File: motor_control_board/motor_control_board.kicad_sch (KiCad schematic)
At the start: 27 parts

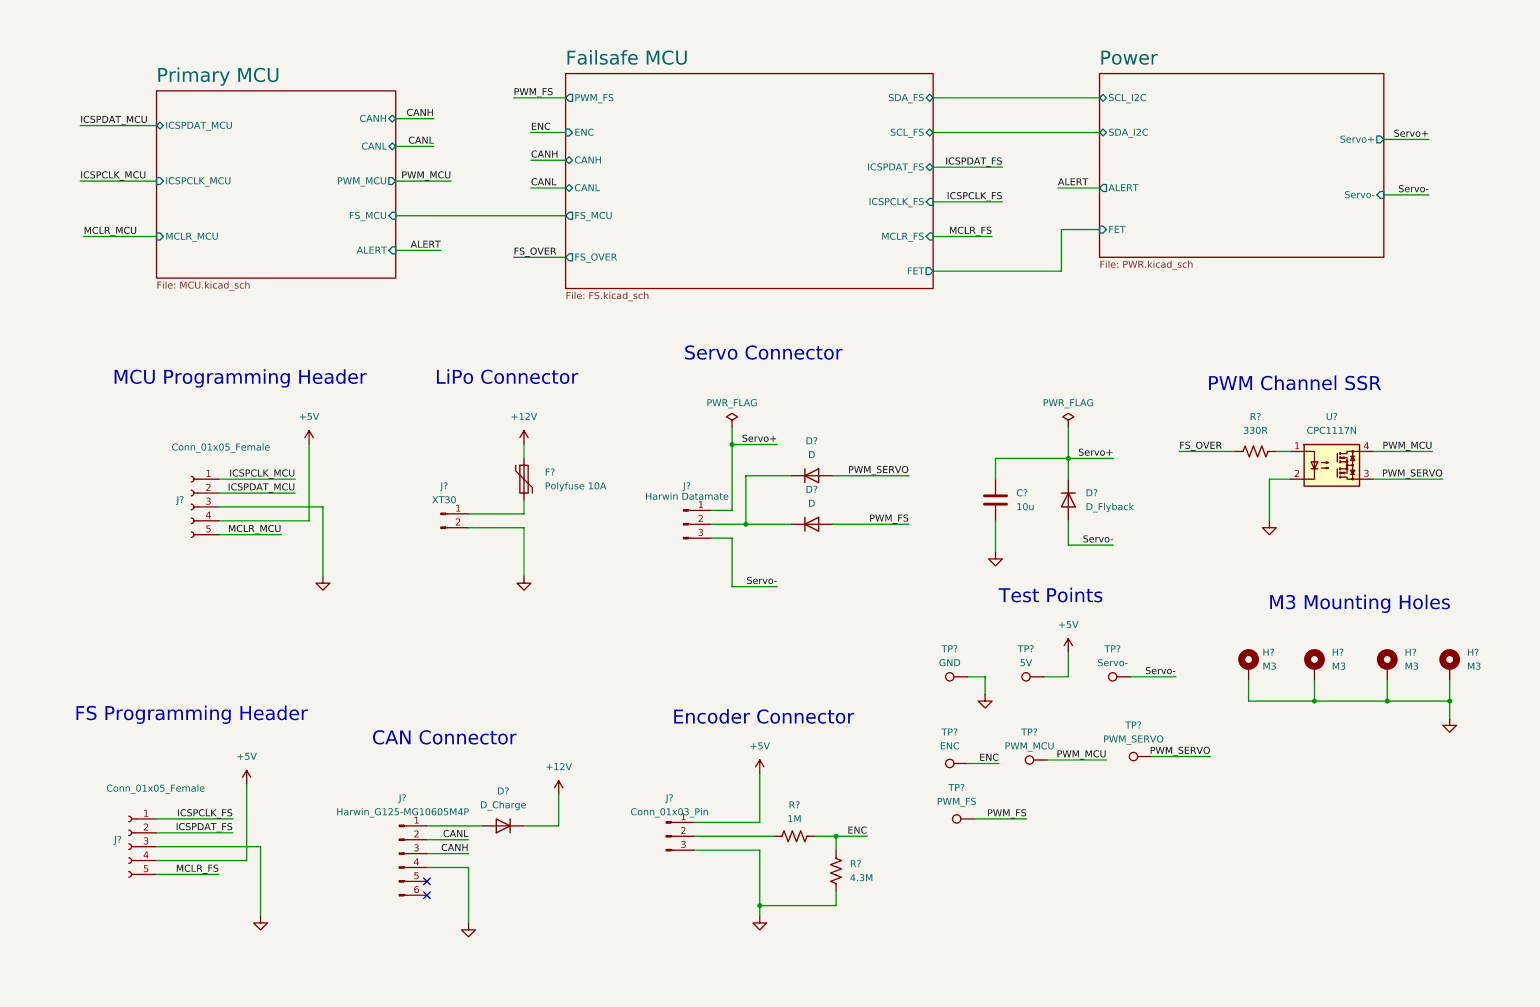
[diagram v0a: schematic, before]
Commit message: Minor schematic edits
Annotated schematic, selected mosfet and diodes, addressed comments
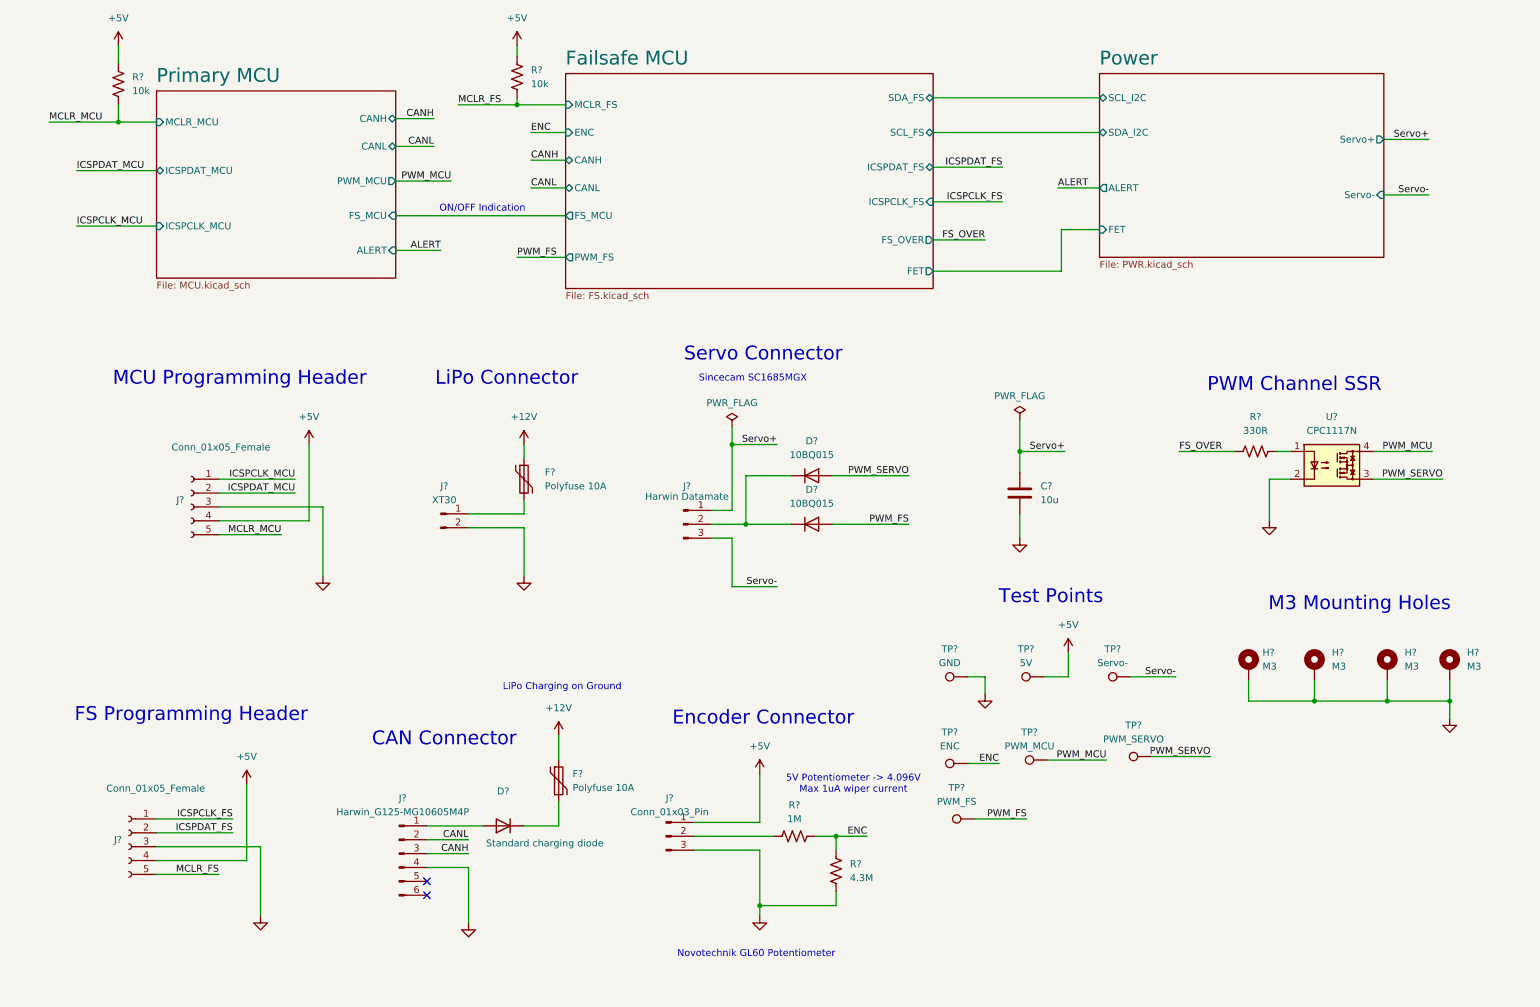
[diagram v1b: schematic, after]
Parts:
- removed D?: D_Flyback, symbol canhw:D
- added F?: Polyfuse 10A, symbol canhw:Polyfuse
- added R? (x2): 10k, symbol Device:R_US
- D? (x2): value D -> 10BQ015
- D?: value D_Charge -> Standard charging diode
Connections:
- net +12V: now also F?.1; no longer D?.1 (K)
- net +5V: now also R?.1, R?.1
- net MCLR_FS: now also R?.2
- net MCLR_MCU: now also R?.2
- new net: D?.1 (K), F?.2
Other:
- note added: "5V Potentiometer -> 4.096V Max 1uA wiper current"
- note added: "LiPo Charging on Ground"
- note added: "Novotechnik GL60 Potentiometer"
- note added: "ON/OFF Indication"
- note added: "Sincecam SC1685MGX"
- moved on the sheet: C?

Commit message: Added second encoder connection, minor edits
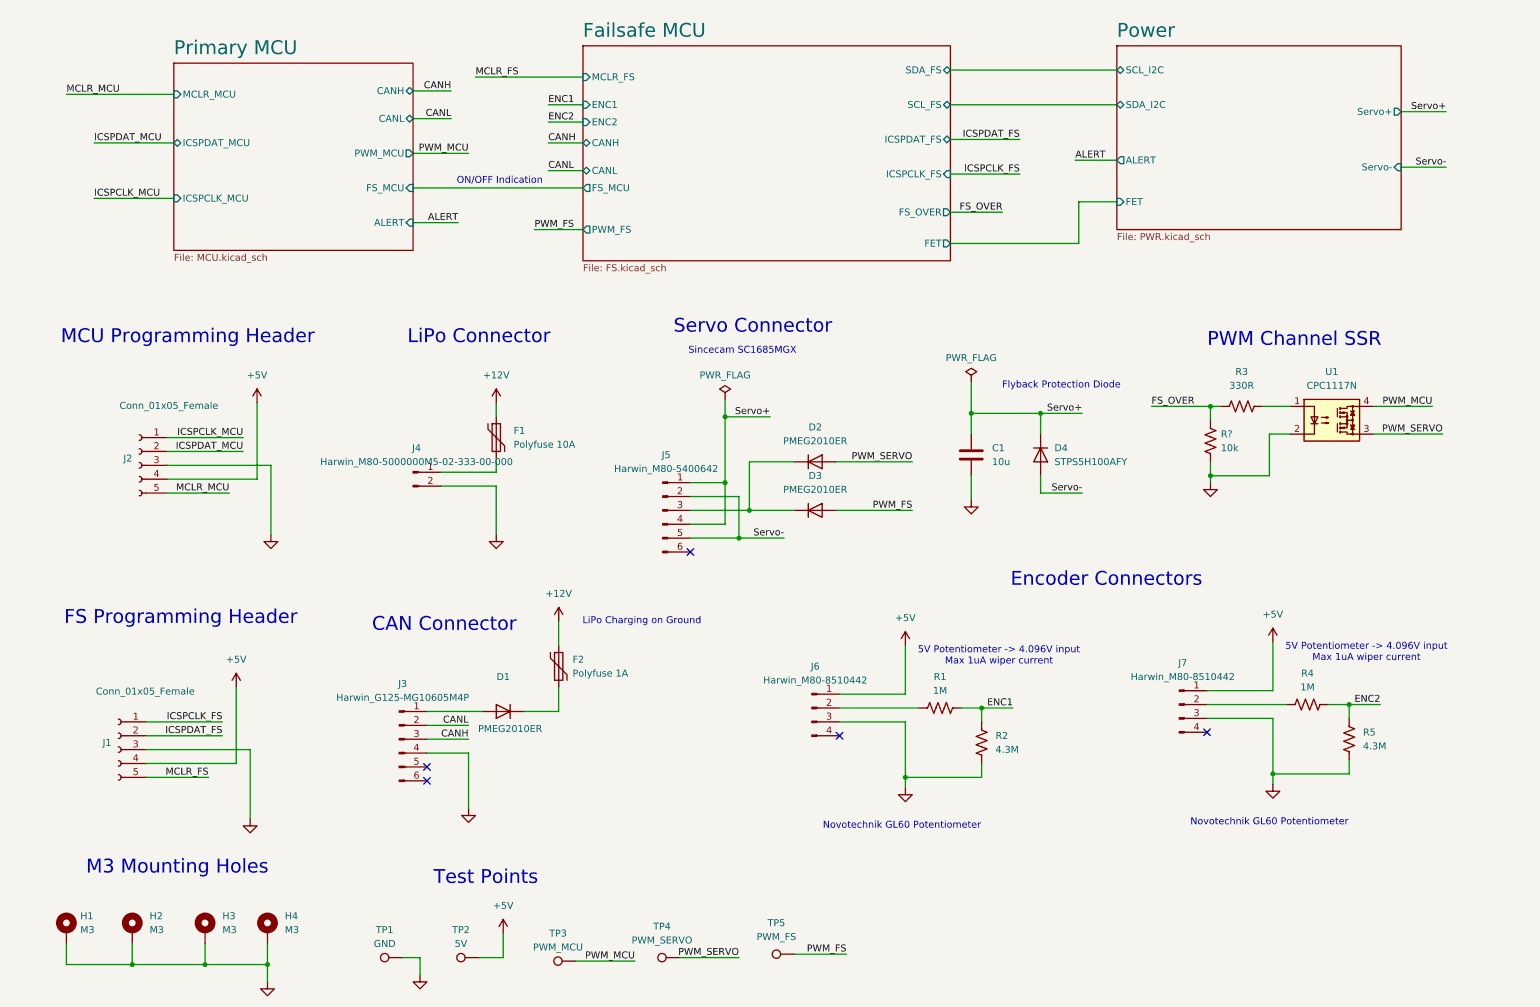
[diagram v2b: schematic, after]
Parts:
- removed J?: Conn_01x03_Pin, symbol canhw:Conn_01x03_Pin
- removed J?: Harwin Datamate, symbol canhw:Conn_01x03_Pin
- removed R? (x2): 10k, symbol Device:R_US
- removed TP?: Servo-, symbol canhw:TestPoint
- removed TP?: ENC, symbol canhw:TestPoint
- added D4: STPS5H100AFY, symbol canhw:D
- added J5: Harwin_M80-5400642, symbol canhw:Conn_01x06_Pin
- added J6, J7: Harwin_M80-8510442, symbol Connector:Conn_01x04_Pin
- added R4: 1M, symbol canhw:R_US
- added R5: 4.3M, symbol canhw:R_US
- added R?: 10k, symbol Device:R_US
- D1: renamed from D?; value Standard charging diode -> PMEG2010ER
- D2, D3: renamed from D?; value 10BQ015 -> PMEG2010ER
- F2: renamed from F?; value Polyfuse 10A -> Polyfuse 1A
- J4: renamed from J?; value XT30 -> Harwin_M80-5000000M5-02-333-00-000
- gave numbers to parts that had none: 18
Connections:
- net +5V: now also J6.1 (Pin_1), J7.1 (Pin_1)
- net FS_OVER: now also R?.1
- net GND: now also J6.3 (Pin_3), J7.3 (Pin_3), R5.2, R?.2
- net Servo+: now also D4.1 (K), J5.1 (Pin_1), J5.4 (Pin_4)
- net Servo-: now also D4.2 (A), J5.2 (Pin_2), J5.5 (Pin_5)
- net at R1.1: now also J6.2 (Pin_2)
- net at D2.1 (K), D3.1 (K): now also J5.3 (Pin_3)
- net ENC renamed ENC1
- new net: J7.2 (Pin_2), R4.1
- new net ENC2: R4.2, R5.1
- no-connect marks 2 -> 5
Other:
- sheet Failsafe MCU ports: added ENC1, ENC2; removed ENC
- note added: "5V Potentiometer -> 4.096V input Max 1uA wiper current"
- note added: "Encoder Connectors"
- note added: "Flyback Protection Diode"
- note removed: "5V Potentiometer -> 4.096V Max 1uA wiper current"
- note removed: "Encoder Connector"
- moved on the sheet: C1, D1, D2, D3, F1, F2, H1, H2, H3, H4, J1, J2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

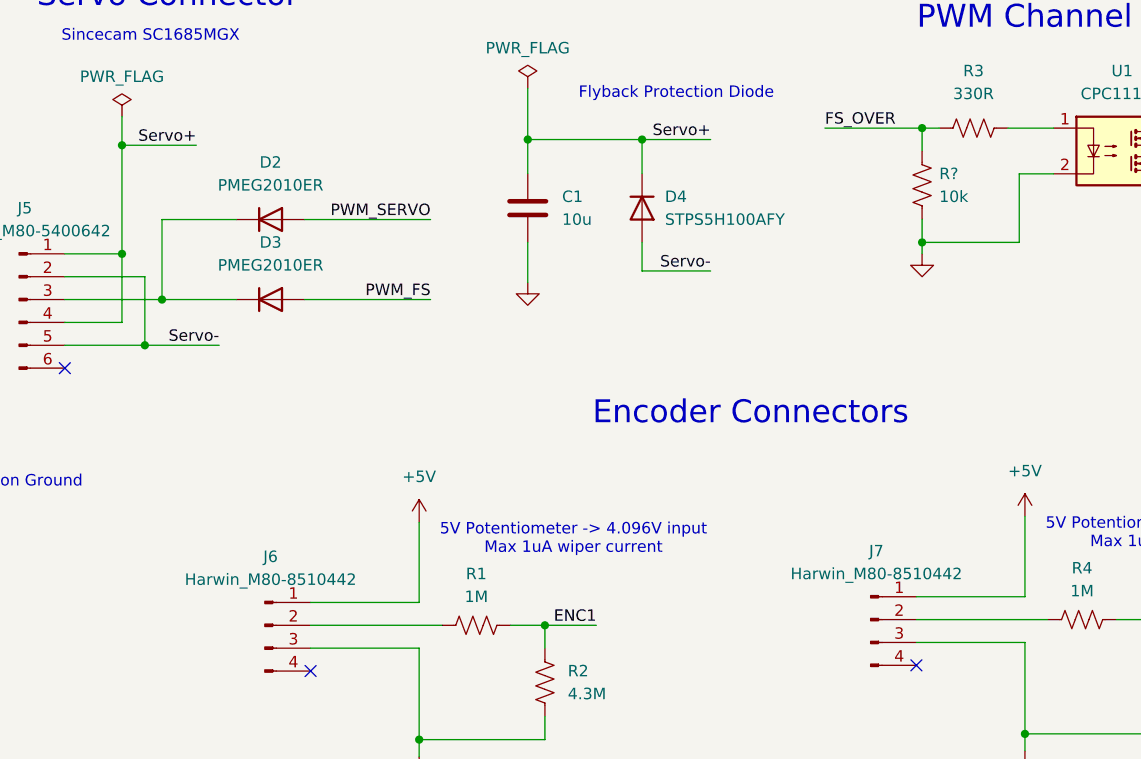
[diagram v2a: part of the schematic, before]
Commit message: assigned footprints
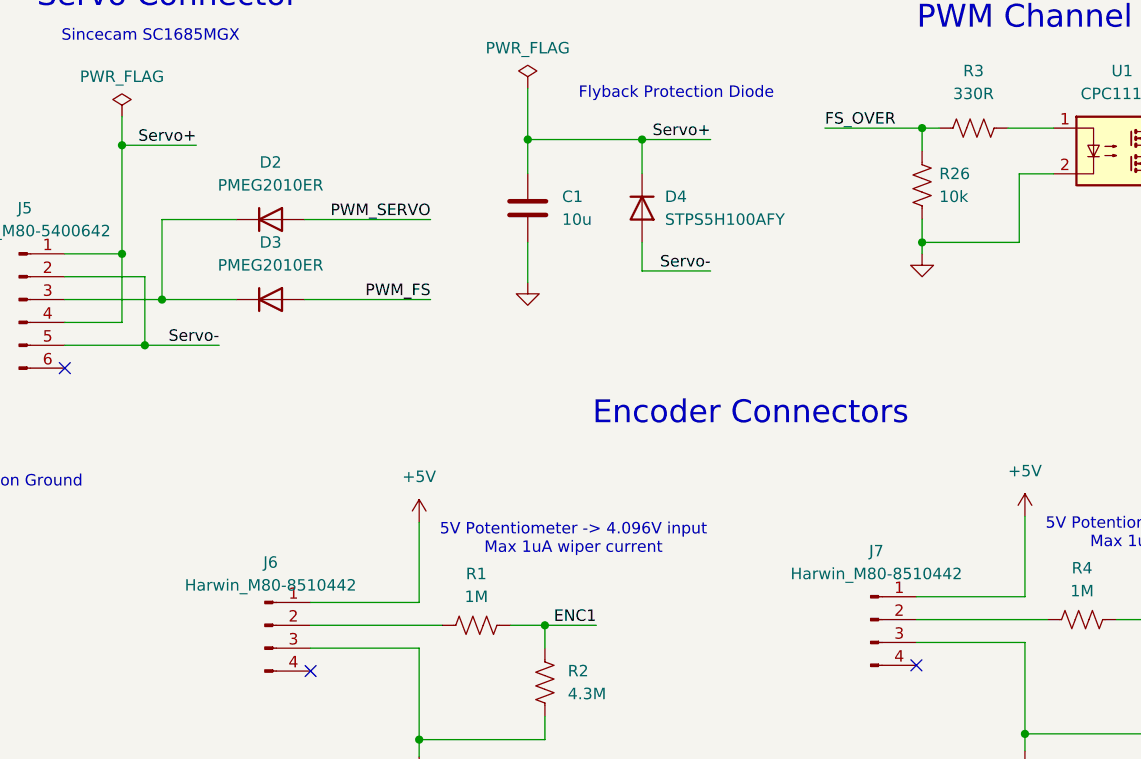
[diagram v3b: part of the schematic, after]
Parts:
- C1: footprint (none) -> Capacitor_SMD:C_0805_2012Metric_Pad1.18x1.45mm_HandSolder
- D1, D2, D3: footprint (none) -> Diode_SMD:Nexperia_CFP3_SOD-123W
- D4: footprint (none) -> Diode_SMD:D_SOD-128
- F1, F2: footprint (none) -> Fuse:Fuse_1206_3216Metric_Pad1.42x1.75mm_HandSolder
- H1, H2, H3, H4: footprint (none) -> MountingHole:MountingHole_3.2mm_M3_DIN965_Pad
- J1, J2: footprint (none) -> canhw_footprints:PinSocket_5x2.54_SMD_90deg_952-3198-1-ND
- J3: footprint (none) -> canhw_footprints:connector_Harwin_G125–MG10605M4P
- J4: footprint (none) -> motor-control:HARWIN_M80-5000000M5-02-333-00-000
- J5: footprint (none) -> motor-control:HARWIN_M80-5400642
- J6, J7: footprint (none) -> motor-control:HARWIN_M80-8510442
- R1, R2, R3, R4, R5: footprint (none) -> Resistor_SMD:R_0805_2012Metric_Pad1.20x1.40mm_HandSolder
- R26: renamed from R?; footprint (none) -> Resistor_SMD:R_0805_2012Metric_Pad1.20x1.40mm_HandSolder
- TP1, TP2, TP3, TP4, TP5: footprint (none) -> TestPoint:TestPoint_Keystone_5000-5004_Miniature
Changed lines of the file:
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@@
 			)
 		)
-		(property "Footprint" ""
+		(property "Footprint" "Fuse:Fuse_1206_3216Metric_Pad1.42x1.75mm_HandSolder"
 			(at 99.695 97.155 0)
 			(effects
@@
 			)
 		)
-		(property "Footprint" ""
+		(property "Footprint" "TestPoint:TestPoint_Keystone_5000-5004_Miniature"
 			(at 153.035 181.61 0)
 			(effects
@@
 			)
 		)
-		(property "Footprint" ""
+		(property "Footprint" "MountingHole:MountingHole_3.2mm_M3_DIN965_Pad"
 			(at 56.515 182.245 0)
 			(effects
@@
 			)
 		)
-		(property "Footprint" ""
+		(property "Footprint" "motor-control:HARWIN_M80-8510442"
 			(at 223.52 140.97 0)
 			(effects
@@
 			)
 		)
-		(property "Footprint" ""
+		(property "Footprint" "motor-control:HARWIN_M80-5000000M5-02-333-00-000"
 			(at 83.185 98.425 0)
 			(effects
@@
 			)
 		)
-		(property "Footprint" ""
+		(property "Footprint" "Fuse:Fuse_1206_3216Metric_Pad1.42x1.75mm_HandSolder"
 			(at 111.125 139.065 0)
 			(effects
@@
 			)
 		)
-		(property "Footprint" ""
+		(property "Footprint" "TestPoint:TestPoint_Keystone_5000-5004_Miniature"
 			(at 95.25 182.245 0)
 			(effects
@@
 		(dnp no)
 		(fields_autoplaced yes)
-		(property "Reference" "R?"
+		(property "Reference" "R26"
 			(at 231.14 91.4399 0)
 			(effects
@@
 			)
 		)
-		(property "Footprint" ""
+		(property "Footprint" "Resistor_SMD:R_0805_2012Metric_Pad1.20x1.40mm_HandSolder"
 			(at 230.251 92.964 90)
 			(effects
@@
 			(project ""
 				(path "/ced26b11-410b-4897-bfe1-68b095b3fef4"
-					(reference "R?")
+					(reference "R26")
 					(unit 1)
 				)
@@
 			)
 		)
-		(property "Footprint" ""
+		(property "Footprint" "Diode_SMD:Nexperia_CFP3_SOD-123W"
 			(at 156.845 105.41 0)
 			(effects
@@
 		(fields_autoplaced yes)
 		(property "Reference" "J6"
-			(at 156.845 133.985 0)
+			(at 156.845 134.62 0)
 			(effects
 				(font
@@
 		)
 		(property "Value" "Harwin_M80-8510442"
-			(at 156.845 136.525 0)
+			(at 156.845 137.16 0)
 			(effects
 				(font
@@
 			)
 		)
-		(property "Footprint" ""
+		(property "Footprint" "motor-control:HARWIN_M80-8510442"
 			(at 156.21 141.605 0)
 			(effects
@@
 			)
 		)
-		(property "Footprint" ""
+		(property "Footprint" "canhw_footprints:PinSocket_5x2.54_SMD_90deg_952-3198-1-ND"
 			(at 33.02 97.155 0)
 			(effects
@@
 			)
 		)
-		(property "Footprint" ""
+		(property "Footprint" "MountingHole:MountingHole_3.2mm_M3_DIN965_Pad"
 			(at 31.75 182.245 0)
 			(effects
@@
 			)
 		)
-		(property "Footprint" ""
+		(property "Footprint" "canhw_footprints:connector_Harwin_G125–MG10605M4P"
 			(at 80.645 147.32 0)
 			(effects
@@
 			)
 		)
-		(property "Footprint" ""
+		(property "Footprint" "MountingHole:MountingHole_3.2mm_M3_DIN965_Pad"
 			(at 45.085 182.245 0)
 			(effects
@@
 			)
 		)
-		(property "Footprint" ""
+		(property "Footprint" "MountingHole:MountingHole_3.2mm_M3_DIN965_Pad"
 			(at 19.685 182.245 0)
 			(effects
@@
 			)
 		)
-		(property "Footprint" ""
+		(property "Footprint" "Resistor_SMD:R_0805_2012Metric_Pad1.20x1.40mm_HandSolder"
 			(at 255.651 147.574 90)
 			(effects
@@
 			)
 		)
-		(property "Footprint" ""
+		(property "Footprint" "Diode_SMD:Nexperia_CFP3_SOD-123W"
 			(at 99.695 142.24 0)
 			(effects
@@
 			)
 		)
-		(property "Footprint" ""
+		(property "Footprint" "motor-control:HARWIN_M80-5400642"
 			(at 128.905 105.41 0)
 			(effects
@@
 			)
 		)
-		(property "Footprint" ""
+		(property "Footprint" "TestPoint:TestPoint_Keystone_5000-5004_Miniature"
 			(at 81.28 182.245 0)
 			(effects
@@
 			)
 		)
-		(property "Footprint" ""
+		(property "Footprint" "TestPoint:TestPoint_Keystone_5000-5004_Miniature"
 			(at 113.03 182.88 0)
 			(effects
@@
 			)
 		)
-		(property "Footprint" ""
+		(property "Footprint" "Diode_SMD:Nexperia_CFP3_SOD-123W"
 			(at 156.845 96.52 0)
 			(effects
@@
 			)
 		)
-		(property "Footprint" ""
+		(property "Footprint" "TestPoint:TestPoint_Keystone_5000-5004_Miniature"
 			(at 132.08 182.245 0)
 			(effects
@@
 			)
 		)
-		(property "Footprint" ""
+		(property "Footprint" "Resistor_SMD:R_0805_2012Metric_Pad1.20x1.40mm_HandSolder"
 			(at 235.204 85.344 90)
 			(effects
@@
 			)
 		)
-		(property "Footprint" ""
+		(property "Footprint" "Resistor_SMD:R_0805_2012Metric_Pad1.20x1.40mm_HandSolder"
 			(at 247.269 139.954 90)
 			(effects
@@
 			)
 		)
-		(property "Footprint" ""
+		(property "Footprint" "Resistor_SMD:R_0805_2012Metric_Pad1.20x1.40mm_HandSolder"
 			(at 179.959 140.589 90)
 			(effects
@@
 			)
 		)
-		(property "Footprint" ""
+		(property "Footprint" "Capacitor_SMD:C_0805_2012Metric_Pad1.18x1.45mm_HandSolder"
 			(at 186.3852 99.06 0)
 			(effects
@@
 			)
 		)
-		(property "Footprint" ""
+		(property "Footprint" "canhw_footprints:PinSocket_5x2.54_SMD_90deg_952-3198-1-ND"
 			(at 29.21 149.225 0)
 			(effects
@@
 			)
 		)
-		(property "Footprint" ""
+		(property "Footprint" "Resistor_SMD:R_0805_2012Metric_Pad1.20x1.40mm_HandSolder"
 			(at 188.341 148.209 90)
 			(effects
@@
 			)
 		)
-		(property "Footprint" ""
+		(property "Footprint" "Diode_SMD:D_SOD-128"
 			(at 198.12 95.25 0)
 			(effects
